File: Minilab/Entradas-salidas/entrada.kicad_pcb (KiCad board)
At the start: 2 copper layers, 61.5 x 68.2 mm, 54 parts, among them J0 In 5V, J1 Out 5V/0V, J10 Vin, J11 Vin, J12 Vin, J13 In 5V, J14 In 5V, J2 Out 5V/0V, J3 Out 5V/0V, J4 Out 5V/0V, J5 Out 5V/0V, J6 Out 5V/0V, J7 Vin, J8 Vin, J9 Vin, SW1 SW_SPST, SW2 SW_SPST, SW3 SW_SPST, SW4 SW_SPST, SW5 SW_SPST, SW6 SW_SPST, SW8 SW_DIP_x07

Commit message: avance pcb y agregado mini360
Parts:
- removed D10, D11, D12, D8, D9: LED, LED_THT:LED_D5.0mm
- removed G*** (x2): LOGO, logoutn:utnkicad2mm
- removed J0: In 5V, Connector_Molex:Molex_KK-254_AE-6410-02A_1x02_P2.54mm_Vertical
- removed SW8: SW_DIP_x07, Package_DIP:DIP-14_W7.62mm_Socket
- added D1: LED, LED_THT:LED_D5.0mm, F.Cu at (108.1, 168.3)
- added D2: LED, LED_THT:LED_D5.0mm, F.Cu at (33.6, 167.1)
- added D3: LED, LED_THT:LED_D5.0mm, F.Cu at (33.6, 160.6)
- added D4: LED, LED_THT:LED_D5.0mm, F.Cu at (33.6, 154.1)
- added D5: LED, LED_THT:LED_D5.0mm, F.Cu at (33.6, 147.6)
- added D6: LED, LED_THT:LED_D5.0mm, F.Cu at (33.6, 141.1)
- added J15: Vin, Connector_PinSocket_2.00mm:PinSocket_1x01_P2.00mm_Vertical, F.Cu at (97.1, 175.4)
- added J16: Vin, Connector_PinSocket_2.00mm:PinSocket_1x01_P2.00mm_Vertical, F.Cu at (98.1, 166.3)
- added JP1: Conn_01x10_Pin, Connector_PinHeader_2.54mm:PinHeader_1x10_P2.54mm_Vertical, F.Cu at (185.0, 76.4)
- added JP2: Conn_01x07_Pin, Connector_PinHeader_2.54mm:PinHeader_1x07_P2.54mm_Vertical, F.Cu at (225.2, 91.9)
- added JP3: Conn_01x06_Pin, Connector_PinHeader_2.54mm:PinHeader_1x06_P2.54mm_Vertical, F.Cu at (225.2, 98.4)
- added JP4: Conn_01x06_Pin, Connector_PinSocket_2.54mm:PinSocket_1x06_P2.54mm_Vertical, F.Cu at (44.1, 144.5)
- added JP5: Conn_01x07_Pin, Connector_PinSocket_2.54mm:PinSocket_1x07_P2.54mm_Vertical, F.Cu at (39.1, 143.2)
- added J_JACK1: Jack-DC, Connector_BarrelJack:BarrelJack_Horizontal, F.Cu at (198.3, 46.9)
- added J_USB1: USB_B_Micro, Connector_USB:USB_Micro-B_Molex_47346-0001, F.Cu at (197.6, 67.1)
- added R13: 2.7K, Resistor_THT:R_Axial_DIN0204_L3.6mm_D1.6mm_P7.62mm_Horizontal, F.Cu at (208.4, 139.8)
- added R14: 470, Resistor_THT:R_Axial_DIN0204_L3.6mm_D1.6mm_P7.62mm_Horizontal, F.Cu at (105.8, 159.8)
- added RV1: 5K, Potentiometer_THT:Potentiometer_Omeg_PC16BU_Horizontal, F.Cu at (109.0, 149.8)
- added U1: 4049, Package_DIP:CERDIP-16_W7.62mm_SideBrazed, F.Cu at (231.1, 68.6)
- added U10: NE555P, Package_DIP:DIP-8_W7.62mm, F.Cu at (232.3, 83.6)
- added U2: Mini360, Mini360:Mini360_step-down, F.Cu at (215.2, 60.0)
- J1, J10, J11, J12, J2, J3, J4, J5, J6, J7, J8, J9: footprint Connector_PinHeader_1.00mm:PinHeader_1x01_P1.00mm_Vertical -> Connector_PinSocket_2.00mm:PinSocket_1x01_P2.00mm_Vertical
- J13: value In 5V -> Vin; footprint Connector_Molex:Molex_KK-254_AE-6410-02A_1x02_P2.54mm_Vertical -> Connector_PinSocket_2.00mm:PinSocket_1x01_P2.00mm_Vertical
- J14: value In 5V -> Conn_01x10_Pin; footprint Connector_Molex:Molex_KK-254_AE-6410-02A_1x02_P2.54mm_Vertical -> Connector_PinSocket_2.54mm:PinSocket_1x10_P2.54mm_Vertical
- SW1, SW2, SW3, SW4, SW5, SW6: footprint Button_Switch_THT:SW_CuK_OS102011MA1QN1_SPDT_Angled -> Button_Switch_THT:SW_Slide_SPDT_Straight_CK_OS102011MS2Q
- moved R12!1 135.5 mm to (226.9, 116.1), turned to 90 degrees
- moved R11!1 131.5 mm to (225.4, 127.2), turned to 90 degrees
- moved R12 131.0 mm to (222.0, 115.6)
- moved R11 127.0 mm to (220.9, 127.8)
- moved J10 112.3 mm to (25.4, 147.6), turned to 180 degrees
- moved J11 110.3 mm to (25.4, 154.1), turned to 180 degrees
- moved J1 110.2 mm to (61.1, 124.3), turned to 0 degrees
- moved J12 109.5 mm to (25.4, 160.6), turned to 180 degrees
- moved R10!1 108.8 mm to (214.4, 115.2), turned to 90 degrees
- moved J2 108.4 mm to (61.1, 128.4), turned to 0 degrees
- moved J3 106.7 mm to (61.1, 132.4), turned to 0 degrees
- moved R7!1 106.3 mm to (200.9, 133.2), turned to 90 degrees
- moved J4 105.3 mm to (61.1, 136.5), turned to 0 degrees
- moved C1 105.0 mm to (71.3, 147.3), turned to 0 degrees
- moved R10 104.7 mm to (210.4, 115.1)
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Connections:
- C1 pad 1: GND1 -> GNDSw
- C1 pad 2: Net-(J1-Pin_1) -> /PinC1
- C2 pad 1: GND1 -> GNDSw
- C2 pad 2: Net-(J2-Pin_1) -> /PinC2
- C3 pad 1: GND1 -> GNDSw
- C3 pad 2: Net-(J3-Pin_1) -> /PinC3
- C4 pad 1: GND1 -> GNDSw
- C4 pad 2: Net-(J4-Pin_1) -> /PinC4
- C5 pad 1: GND1 -> GNDSw
- C5 pad 2: Net-(J5-Pin_1) -> /PinC5
- C6 pad 1: GND1 -> GNDSw
- C6 pad 2: Net-(J6-Pin_1) -> /PinC6
- D7 pad 1: Net-(D7-K) -> /PinFOut1
- D7 pad 2: +5V -> VCCLed
- J1 pad 1: Net-(J1-Pin_1) -> /PinC1
- J10 pad 1: Net-(J10-Pin_1) -> /PinDIn1
- J11 pad 1: Net-(J11-Pin_1) -> /PinCIn1
- J12 pad 1: Net-(J12-Pin_1) -> /PinBIn1
- J13 pad 1: GND -> /PinAIn1
- J14 pad 1: +5V -> /PinC1
- J14 pad 2: GND -> /PinC2
- J2 pad 1: Net-(J2-Pin_1) -> /PinC2
- J3 pad 1: Net-(J3-Pin_1) -> /PinC3
- J4 pad 1: Net-(J4-Pin_1) -> /PinC4
- J5 pad 1: Net-(J5-Pin_1) -> /PinC5
- J6 pad 1: Net-(J6-Pin_1) -> /PinC6
- J7 pad 1: Net-(J7-Pin_1) -> VCCLed
- J8 pad 1: Net-(J8-Pin_1) -> /PinFIn1
- J9 pad 1: Net-(J9-Pin_1) -> /PinEIn1
- R1 pad 2: Net-(J1-Pin_1) -> /PinR1
- R10 pad 1: Net-(J10-Pin_1) -> GND
- R10 pad 2: GND -> /PinDIn
- R10!1 pad 2: Net-(R10!1-Pad2) -> /PinDOut
- R11 pad 1: Net-(J11-Pin_1) -> GND
- R11 pad 2: GND -> /PinEIn
- R11!1 pad 2: Net-(R11!1-Pad2) -> /PinEOut
- R12 pad 1: Net-(J12-Pin_1) -> GND
- R12 pad 2: GND -> /PinFIn
- R12!1 pad 2: Net-(R12!1-Pad2) -> /PinFOut
- R2 pad 2: Net-(J2-Pin_1) -> /PinR2
- R3 pad 2: Net-(J3-Pin_1) -> /PinR3
- R4 pad 2: Net-(J4-Pin_1) -> /PinR4
- R5 pad 2: Net-(J5-Pin_1) -> /PinR5
- R6 pad 2: Net-(J6-Pin_1) -> /PinR6
- R7 pad 2: Net-(J7-Pin_1) -> /PinAIn
- R7!1 pad 2: Net-(D7-K) -> /PinAOut
- R8 pad 2: Net-(J8-Pin_1) -> /PinBIn
- R8!1 pad 2: Net-(D8-K) -> /PinBOut
- R9 pad 2: Net-(J9-Pin_1) -> /PinCIn
- R9!1 pad 2: Net-(D9-K) -> /PinCOut
- SW1 pad 1: Net-(J1-Pin_1) -> /PinC1
- SW1 pad 2: GND1 -> GNDSw
- SW2 pad 1: Net-(J2-Pin_1) -> /PinC2
- SW2 pad 2: GND1 -> GNDSw
- SW3 pad 1: Net-(J3-Pin_1) -> /PinC3
- SW3 pad 2: GND1 -> GNDSw
- SW4 pad 1: Net-(J4-Pin_1) -> /PinC4
- SW4 pad 2: GND1 -> GNDSw
- SW5 pad 1: Net-(J5-Pin_1) -> /PinC5
- SW5 pad 2: GND1 -> GNDSw
- SW6 pad 1: Net-(J6-Pin_1) -> /PinC6
- SW6 pad 2: GND1 -> GNDSw
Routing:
- net +5V: track 152.6 -> 0.00 mm
- net VCC: track 53.7 -> 0.00 mm
- net VCCLed: track 0.00 -> 53.1 mm
- net /PinDIn1: track 0.00 -> 50.8 mm
- net /PinCIn1: track 0.00 -> 50.3 mm
- net /PinEIn1: track 0.00 -> 45.2 mm
- net /PinBIn1: track 0.00 -> 44.3 mm
- net /PinFIn1: track 0.00 -> 39.3 mm
- net /PinAIn1: track 0.00 -> 38.0 mm
- net Net-(J1-Pin_1): track 31.5 -> 0.00 mm
- net Net-(J3-Pin_1): track 30.1 -> 0.00 mm
- net Net-(J4-Pin_1): track 29.5 -> 0.00 mm
- net Net-(J2-Pin_1): track 29.5 -> 0.00 mm
- net Net-(J5-Pin_1): track 28.7 -> 0.00 mm
- net Net-(J6-Pin_1): track 28.1 -> 0.00 mm
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- removed copper zone on B.Cu, net +5V
- removed copper zone on B.Cu, net GND
- removed copper zone on B.Cu, net GND1
- removed copper zone on B.Cu, net VCC
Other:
- board outline removed
- board text removed: "+5V"
- board text removed: "1"
- board text removed: "A.P."
- board text removed: "MiniLab"

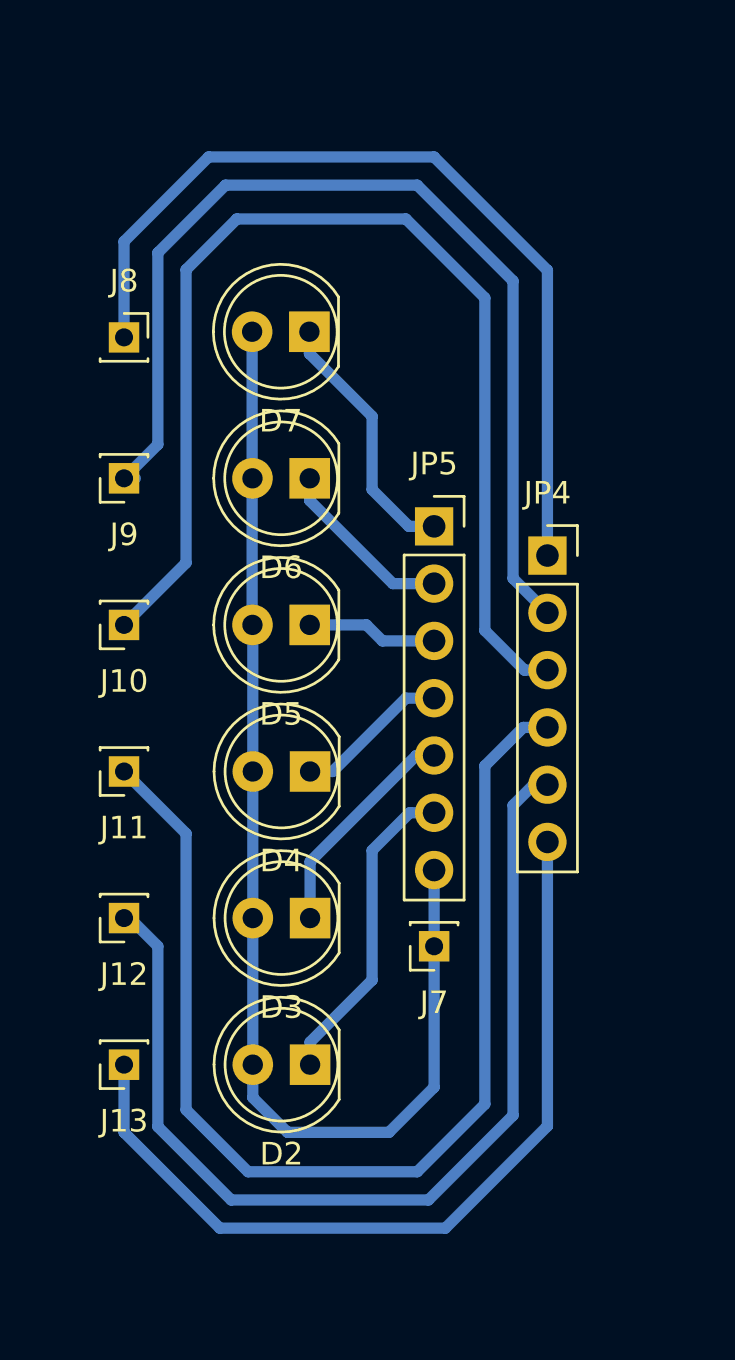
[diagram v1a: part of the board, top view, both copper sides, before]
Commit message: reordenado de led y pines placa sec
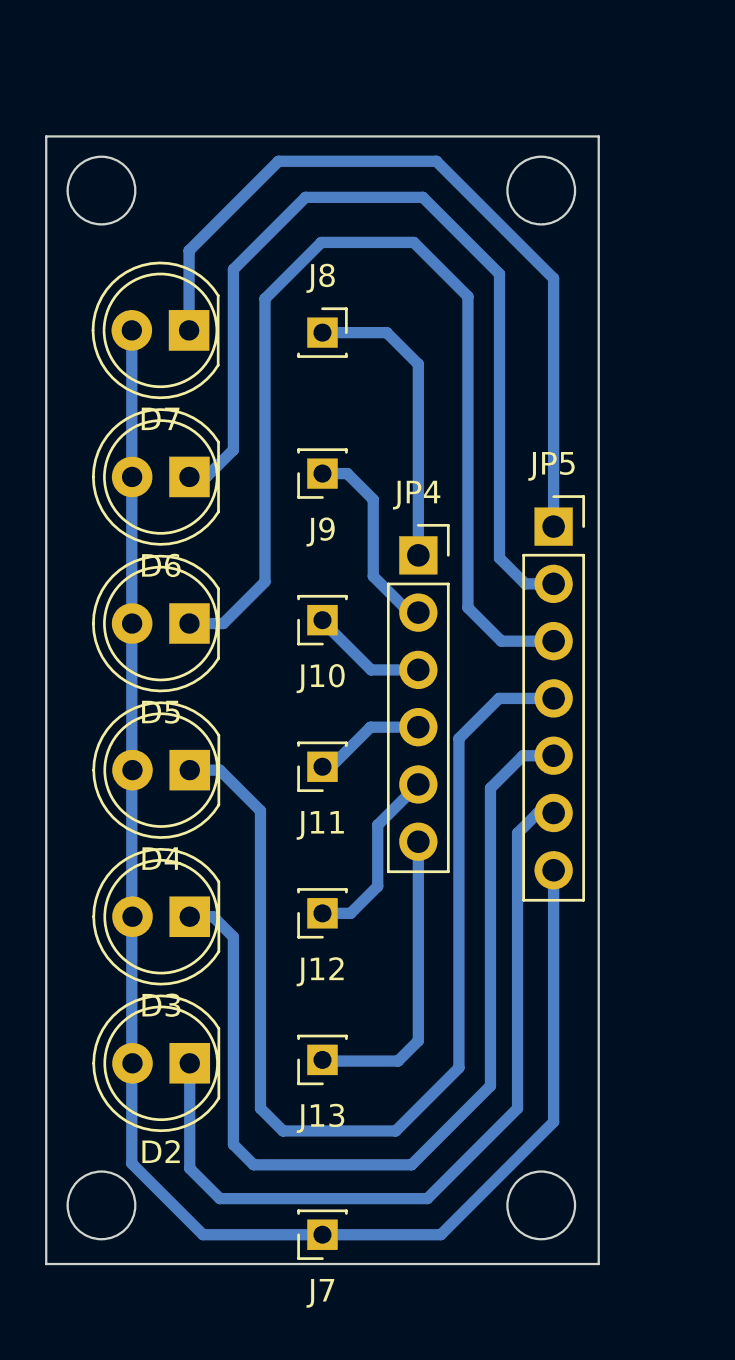
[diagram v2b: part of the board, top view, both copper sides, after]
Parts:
- moved J7 13.7 mm to (34.1, 174.6)
- moved J10 8.80 mm to (34.1, 147.3)
- moved J11 8.80 mm to (34.1, 153.8)
- moved J12 8.80 mm to (34.1, 160.3)
- moved J13 8.80 mm to (34.1, 166.8)
- moved J8 8.80 mm to (34.1, 134.6)
- moved J9 8.80 mm to (34.1, 140.8)
- moved JP4 5.73 mm to (38.4, 144.5)
- moved D2 5.34 mm to (28.3, 167.0)
- moved D3 5.34 mm to (28.3, 160.5)
- moved D4 5.34 mm to (28.3, 154.0)
- moved D5 5.34 mm to (28.2, 147.5)
- moved D6 5.34 mm to (28.2, 141.0)
- moved D7 5.34 mm to (28.2, 134.5)
- moved JP5 5.30 mm to (44.4, 143.2)
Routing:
- net /PinCIn1: track 50.3 -> 5.02 mm
- net /PinDIn1: track 50.8 -> 5.71 mm
- net /PinCOut1: track 6.85 -> 47.0 mm
- net /PinDOut1: track 5.81 -> 45.9 mm
- net /PinEIn1: track 45.2 -> 8.80 mm
- net /PinBIn1: track 44.3 -> 8.21 mm
- net /PinEOut1: track 8.03 -> 40.5 mm
- net /PinBOut1: track 9.95 -> 41.3 mm
- net /PinFIn1: track 39.3 -> 13.3 mm
- net /PinAIn1: track 38.0 -> 13.5 mm
- net /PinFOut1: track 11.6 -> 34.5 mm
- net /PinAOut1: track 14.1 -> 35.6 mm
- net VCCLed: track 53.1 -> 70.2 mm
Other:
- board outline added: 24.5 x 50 mm

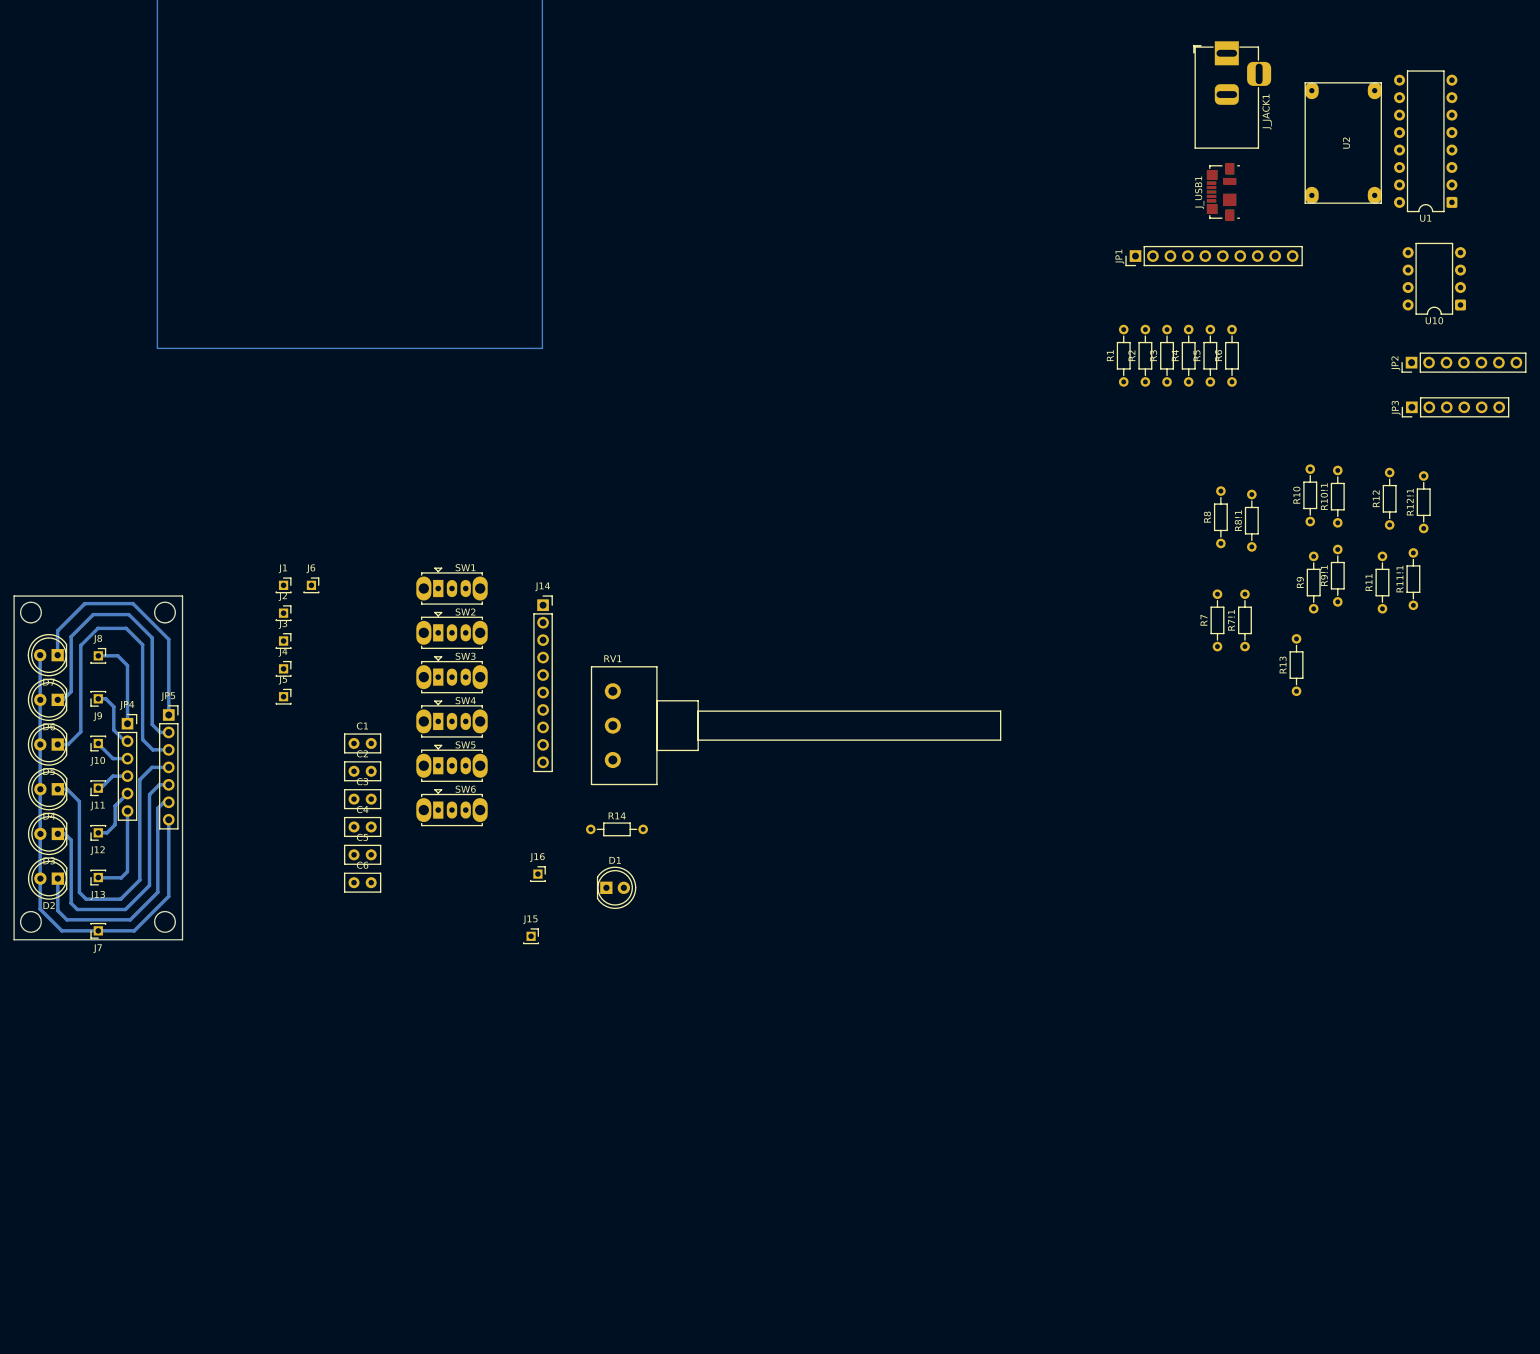
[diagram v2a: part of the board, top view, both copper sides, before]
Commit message: avance placa sec con switches
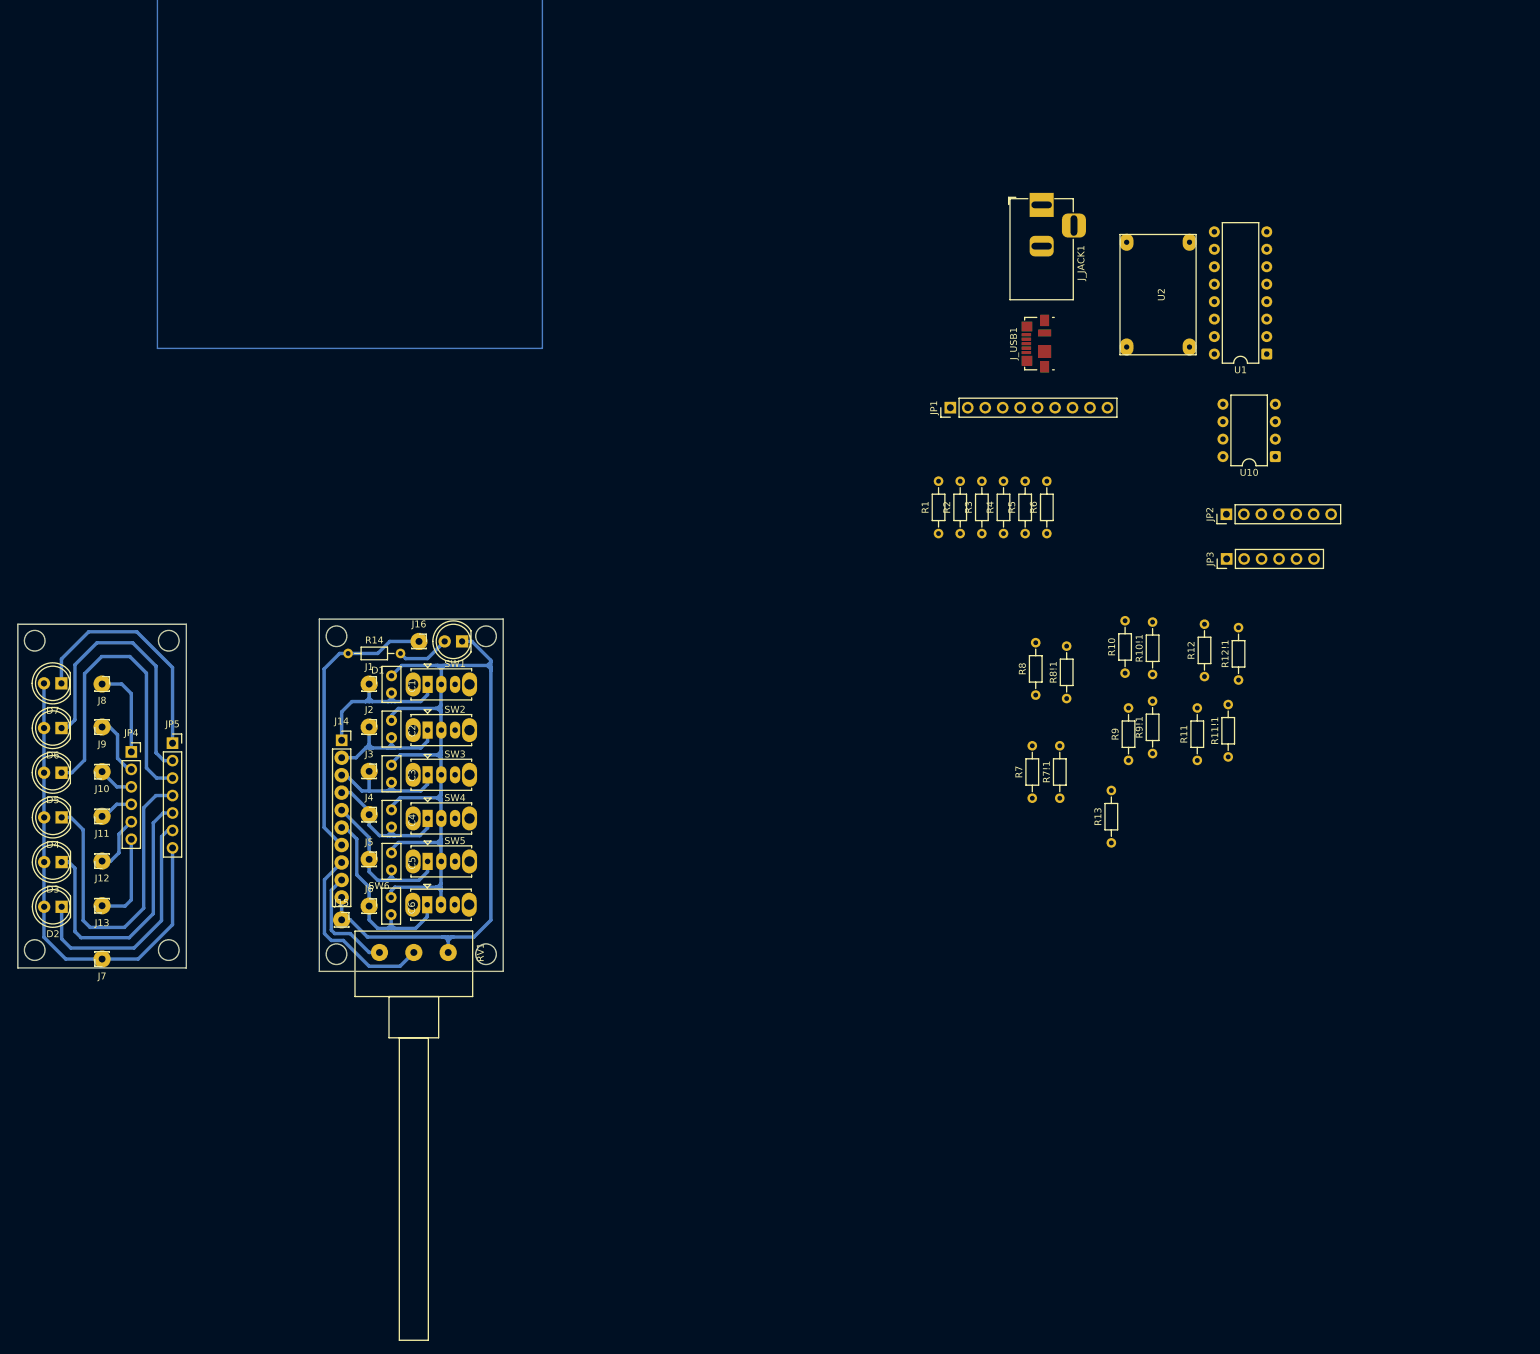
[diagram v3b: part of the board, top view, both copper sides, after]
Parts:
- moved J6 47.4 mm to (73.5, 171.0)
- moved RV1 44.0 mm to (75.0, 177.8), turned to -90 degrees
- moved R14 43.6 mm to (70.5, 134.2)
- moved D1 41.5 mm to (87.1, 132.5), turned to 180 degrees
- moved J16 38.0 mm to (80.8, 132.5)
- moved J14 35.3 mm to (69.5, 146.9)
- moved JP1 34.8 mm to (158.1, 98.5)
- moved JP2 34.8 mm to (198.2, 114.0)
- moved JP3 34.8 mm to (198.3, 120.5)
- moved J_USB1 34.8 mm to (170.6, 89.2)
- moved R1 34.8 mm to (156.4, 116.8)
- moved R10 34.8 mm to (183.5, 137.1)
- moved R10!1 34.8 mm to (187.5, 137.3)
- moved R11 34.8 mm to (194.0, 149.8)
- moved R11!1 34.8 mm to (198.5, 149.3)
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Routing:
- net GNDSw: track 0.00 -> 176.8 mm
- net /OscOut1: track 0.00 -> 42.9 mm
- net /PinC6: track 0.00 -> 30.3 mm
- net /PinPotOut1: track 0.00 -> 27.2 mm
- net /PinC1: track 0.00 -> 26.6 mm
- net /PinC5: track 0.00 -> 25.4 mm
- net /PinC4: track 0.00 -> 23.0 mm
- net /PinC2: track 0.00 -> 22.5 mm
- net /PinC3: track 0.00 -> 22.2 mm
- net VCCSw: track 0.00 -> 16.3 mm
- net Net-(D1-A): track 0.00 -> 7.77 mm
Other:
- board size 24.5 x 50 mm -> 70.6 x 51.2 mm
